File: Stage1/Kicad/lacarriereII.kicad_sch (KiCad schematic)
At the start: 75 parts, among them J1 USB_C_Receptacle_USB2.0, J2 Conn_02x06, J4 Conn_01x06_Pin, U1 PCA9557PW, U10 XC6206P132MR, U11 ESP32_WROVER, U13 BME280, U15 BME280, U2 BQ25171QWDRCRQ1, U3 CH340C, U4 UMH3N, U5 SIM800L-CORE, U6 FS8205, U7 HY2112, U8 TLV61070A, U9 XC6206P282MR

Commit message: [add] mounting holes + custom footprints lib
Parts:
- added H1, H2, H3: MountingHole_Pad, MountingHole:MountingHole_3.2mm_M3_Pad_Via, symbol Mechanical:MountingHole_Pad
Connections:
- net GND: now also H1.1, H2.1, H3.1
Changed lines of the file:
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@@
   (junction (at 167.64 170.18) (diameter 0) (color 0 0 0 0)
   )
+  (junction (at 259.08 246.38) (diameter 0) (color 0 0 0 0)
+  )
   (junction (at 76.2 187.96) (diameter 0) (color 0 0 0 0)
   )
@@
   (junction (at 392.43 167.64) (diameter 0) (color 0 0 0 0)
   )
+  (junction (at 266.7 246.38) (diameter 0) (color 0 0 0 0)
+  )
   (junction (at 22.86 227.33) (diameter 0) (color 0 0 0 0)
   )
@@
     (stroke (width 0) (type default))
   )
+  (wire (pts (xy 266.7 246.38) (xy 266.7 262.89))
+    (stroke (width 0) (type default))
+  )
   (wire (pts (xy 193.04 243.84) (xy 201.93 243.84))
     (stroke (width 0) (type default))
@@
     (stroke (width 0) (type default))
   )
+  (wire (pts (xy 266.7 246.38) (xy 266.7 242.57))
+    (stroke (width 0) (type default))
+  )
   (wire (pts (xy 54.61 242.57) (xy 73.66 242.57))
     (stroke (width 0) (type default))
@@
     (stroke (width 0) (type default))
   )
+  (wire (pts (xy 259.08 246.38) (xy 266.7 246.38))
+    (stroke (width 0) (type default))
+  )
   (wire (pts (xy 52.07 81.28) (xy 59.69 81.28))
     (stroke (width 0) (type default))
@@
     (stroke (width 0) (type default))
   )
+  (wire (pts (xy 259.08 246.38) (xy 259.08 242.57))
+    (stroke (width 0) (type default))
+  )
   (wire (pts (xy 167.64 167.64) (xy 167.64 170.18))
     (stroke (width 0) (type default))
@@
     (stroke (width 0) (type default))
   )
+  (wire (pts (xy 252.73 246.38) (xy 252.73 242.57))
+    (stroke (width 0) (type default))
+  )
   (wire (pts (xy 298.45 187.96) (xy 313.69 187.96))
     (stroke (width 0) (type default))
@@
     (stroke (width 0) (type default))
   )
+  (wire (pts (xy 252.73 246.38) (xy 259.08 246.38))
+    (stroke (width 0) (type default))
+  )
   (wire (pts (xy 118.11 74.93) (xy 118.11 73.66))
     (stroke (width 0) (type default))
@@
     )
   )
+  (symbol (lib_id "power:GND") (at 266.7 262.89 0) (unit 1)
+    (in_bom yes) (on_board yes) (dnp no) (fields_autoplaced)
+    (property "Reference" "#PWR016" (at 266.7 269.24 0)
+      (effects (font (size 1.27 1.27)) hide)
+    )
+    (property "Value" "GND" (at 266.7 267.97 0)
+      (effects (font (size 1.27 1.27)))
+    )
+    (property "Footprint" "" (at 266.7 262.89 0)
+      (effects (font (size 1.27 1.27)) hide)
+    )
+    (property "Datasheet" "" (at 266.7 262.89 0)
+      (effects (font (size 1.27 1.27)) hide)
+    )
+    (pin "1")
+    (instances
+      (project "lacarriereII"
+        (path "/3c8426f4-ef7d-418b-9048-6c57d75d81b5"
+          (reference "#PWR016") (unit 1)
+        )
+      )
+    )
+  )
   (symbol (lib_id "Device:Thermistor_NTC") (at 182.88 163.83 0) (unit 1)
     (in_bom yes) (on_board yes) (dnp no)
@@
     )
   )
+  (symbol (lib_id "Mechanical:MountingHole_Pad") (at 252.73 240.03 0) (unit 1)
+    (in_bom yes) (on_board yes) (dnp no)
+    (property "Reference" "H1" (at 255.27 238.125 0)
+      (effects (font (size 1.27 1.27)) (justify left))
+    )
+    (property "Value" "MountingHole_Pad" (at 261.62 238.76 0)
+      (effects (font (size 1.27 1.27)) (justify left) hide)
+    )
+    (property "Footprint" "MountingHole:MountingHole_3.2mm_M3_Pad_Via" (at 252.73 240.03 0)
+      (effects (font (size 1.27 1.27)) hide)
+    )
+    (property "Datasheet" "~" (at 252.73 240.03 0)
+      (effects (font (size 1.27 1.27)) hide)
+    )
+    (pin "1")
+    (instances
+      (project "lacarriereII"
+        (path "/3c8426f4-ef7d-418b-9048-6c57d75d81b5"
+          (reference "H1") (unit 1)
+        )
+      )
+    )
+  )
   (symbol (lib_id "Connector:TestPoint") (at 279.4 149.86 0) (unit 1)
     (in_bom yes) (on_board yes) (dnp no)
@@
     )
   )
+  (symbol (lib_id "Mechanical:MountingHole_Pad") (at 259.08 240.03 0) (unit 1)
+    (in_bom yes) (on_board yes) (dnp no) (fields_autoplaced)
+    (property "Reference" "H2" (at 261.62 238.125 0)
+      (effects (font (size 1.27 1.27)) (justify left))
+    )
+    (property "Value" "MountingHole_Pad" (at 261.62 240.665 0)
+      (effects (font (size 1.27 1.27)) (justify left) hide)
+    )
+    (property "Footprint" "MountingHole:MountingHole_3.2mm_M3_Pad_Via" (at 259.08 240.03 0)
+      (effects (font (size 1.27 1.27)) hide)
+    )
+    (property "Datasheet" "~" (at 259.08 240.03 0)
+      (effects (font (size 1.27 1.27)) hide)
+    )
+    (pin "1")
+    (instances
+      (project "lacarriereII"
+        (path "/3c8426f4-ef7d-418b-9048-6c57d75d81b5"
+          (reference "H2") (unit 1)
+        )
+      )
+    )
+  )
   (symbol (lib_id "Device:L") (at 220.98 142.24 90) (unit 1)
     (in_bom yes) (on_board yes) (dnp no)
@@
         )
       )
+    )
+  )
+  (symbol (lib_id "Mechanical:MountingHole_Pad") (at 266.7 240.03 0) (unit 1)
+    (in_bom yes) (on_board yes) (dnp no) (fields_autoplaced)
+    (property "Reference" "H3" (at 269.24 238.125 0)
+      (effects (font (size 1.27 1.27)) (justify left))
+    )
+    (property "Value" "MountingHole_Pad" (at 269.24 240.665 0)
+      (effects (font (size 1.27 1.27)) (justify left) hide)
+    )
+    (property "Footprint" "MountingHole:MountingHole_3.2mm_M3_Pad_Via" (at 266.7 240.03 0)
+      (effects (font (size 1.27 1.27)) hide)
+    )
+    (property "Datasheet" "~" (at 266.7 240.03 0)
+      (effects (font (size 1.27 1.27)) hide)
+    )
+    (pin "1")
+    (instances
+      (project "lacarriereII"
+        (path "/3c8426f4-ef7d-418b-9048-6c57d75d81b5"
+          (reference "H3") (unit 1)
+        )
+      )

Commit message: [update] Stage1 schematic after olli's review
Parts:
- removed C20: 1u(nc), Capacitor_SMD:C_0805_2012Metric_Pad1.18x1.45mm_HandSolder, symbol Device:C
- removed R26: 1M, Resistor_SMD:R_0805_2012Metric_Pad1.20x1.40mm_HandSolder, symbol Meteo_Lacarriere:R
- removed U13, U15: BME280, Package_LGA:Bosch_LGA-8_2.5x2.5mm_P0.65mm_ClockwisePinNumbering, symbol Meteo_Lacarriere:BME280
- added C11: NC(1u), Capacitor_SMD:C_0805_2012Metric_Pad1.18x1.45mm_HandSolder, symbol Device:C
- added C13, C14: 1u, Capacitor_SMD:C_0805_2012Metric_Pad1.18x1.45mm_HandSolder, symbol Device:C
- added C21, C23, C24, C3: 0.1u, Capacitor_SMD:C_0805_2012Metric_Pad1.18x1.45mm_HandSolder, symbol Device:C
- added R1: 10k, Resistor_SMD:R_0805_2012Metric_Pad1.20x1.40mm_HandSolder, symbol Meteo_Lacarriere:R
- added R2: 10k, Resistor_SMD:R_0805_2012Metric_Pad1.20x1.40mm_HandSolder, symbol Device:R
- added R24: 1M, Resistor_SMD:R_0805_2012Metric_Pad1.20x1.40mm_HandSolder, symbol Meteo_Lacarriere:R
- added U14, U16: BME280, Package_LGA:Bosch_LGA-8_2.5x2.5mm_P0.65mm_ClockwisePinNumbering, symbol Meteo_Lacarriere:BME280
- added U2: USBLC6-2SC6, Package_TO_SOT_SMD:SOT-23-6_Handsoldering, symbol Meteo_Lacarriere:USBLC6-2SC6
- TH1: value NTC -> NC(NTC)
- renumbered 1V3 to 1V1, 2V8 to 2V1, 3V3 to 3V1, C3 to C1, C11 to C12, C12 to C15, C13 to C16, C14 to C17, C15 to C18, C1 to C19, C16 to C20, C17 to C22, C18 to C25, C19 to C26, J4 to J3, R7 to R10, R8 to R11, R11 to R12, R14 to R13, R12 to R14, R13 to R15, R17 to R16, R15 to R17, R16 to R18, R18 to R19, R19 to R20, R20 to R21, R27 to R22, R25 to R23, R21 to R25, R22 to R26, R23 to R27, R24 to R28, R2 to R5, R9 to R6, R10 to R7, R5 to R8, R6 to R9, U9 to U10, U10 to U11, U11 to U12, U12 to U13, U14 to U15, U16 to U17, U2 to U3, U3 to U4, U4 to U6, U6 to U7, U7 to U8, U8 to U9
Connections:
- net IO0 is gone; now on net IO0_AND_D5: U12.25 (IO0), U6.3 (C2)
- net +3.3V: now also R25.1, R26.2, C13.1, C14.1, C21.1, C23.1, C24.1, C3.1, R1.1, R2.2, U14.2 (~{CS}), U14.6 (VDDIO), U14.8 (VDD), U16.2 (~{CS}), U16.5 (SDO), U16.6 (VDDIO), U16.8 (VDD), U2.5 (VBUS)
- net D3: now also U12.24 (IO2); no longer U12.23 (IO15)
- net DVP_SCL: now also R26.1; no longer R26.2
- net DVP_SDA: now also R25.2; no longer R25.1
- net GND: now also J1.S1 (SHIELD), C11.2, C13.2, C14.2, C21.2, C23.2, C24.2, C3.2, R24.2, U14.1 (GND1), U14.5 (SDO), U14.7 (GND2), U16.1 (GND1), U16.7 (GND2), U2.2 (GND); no longer R25.2, R26.1
- net I2C_SCL: now also R1.2, U14.4 (SCL), U16.4 (SCL)
- net I2C_SDA: now also R2.1, U14.3 (SDA), U16.3 (SDA)
- net VMEAS: now also C11.1, R24.1
- net at R6.2: now also U2.1 (I/O1_1); no longer U4.5 (UD+)
- net IO_EXT2: now reaches J2.11 (Pin_11)
- net IO_EXT2: now also J2.5 (Pin_5), U12.23 (IO15)
- net at U4.6 (UD-): now also U2.4 (I/O2_2); no longer R7.2
- net D5 renamed IO0_AND_D5
- net IO0_AND_D5: no longer U12.37 (IO23)
- net IO2 renamed IO_EXT1
- net IO_EXT1: now also U12.37 (IO23); no longer U12.24 (IO2)
- new net: U2.6 (I/O1_2), U4.5 (UD+)
- new net: R7.2, U2.3 (I/O2_1)
- no-connect marks 13 -> 10
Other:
- note added: "Dual Bosh sensors"
- note added: "Manual jumper selection"
- note added: "R22 populated if no NTC"
- note added: "R27=((Vout/Vref)-1)*R28 R27=((4.1/0.5)-1)*R28 R27=100k ; R28=14k"
- note added: "R3 = 750R ; Charging 0.4A R9=0 ; R10=NC ; NO TEMPERATURE MANAGEMENT R13=62k ; Li+ No Timer R16=100k ; LiFePo4 3.5V charging"
- note added: "USB C 2.0 & Serial programmer"
- note added: "Voltage divider (VMEAS, PIN 4) on ADC1 as ADC2 is OFF when Wifi is active"
- note removed: "Double Bosh sensors"
- note removed: "Manual input selection"
- note removed: "Pont diviseur (VMEAS, PIN 4) sur ADC1 car ADC2 OFF quand WIFI actif"
- note removed: "R23=((Vout/Vref)-1)*R24 R23=((4.1/0.5)-1)*R24 R23=82k ; R24=11.5k L1 74438357022 from Wurth trouver equivalent ?"
- note removed: "R27 populated if no NTC"
- note removed: "R6 = 375R ; Charging 0.8A R10=0 ; R11=NC ; TEMP 0°C to 40°C R16=62k ; Li+ No Timer R17=100k ; LiFePo4 3.5V charging"
- note removed: "USB C & Serial programmer"
- moved on the sheet: 1V1, 2V1, 3V1, 4V1, C1, C15, C16, C17, C18, C19, C2, C20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

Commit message: [fix] a few mistakes on schematic ... ready to reroute!
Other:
- note added: "I2C general pull-ups"
- moved on the sheet: H1, H2, H3, R1, R2, R8, R9, U1

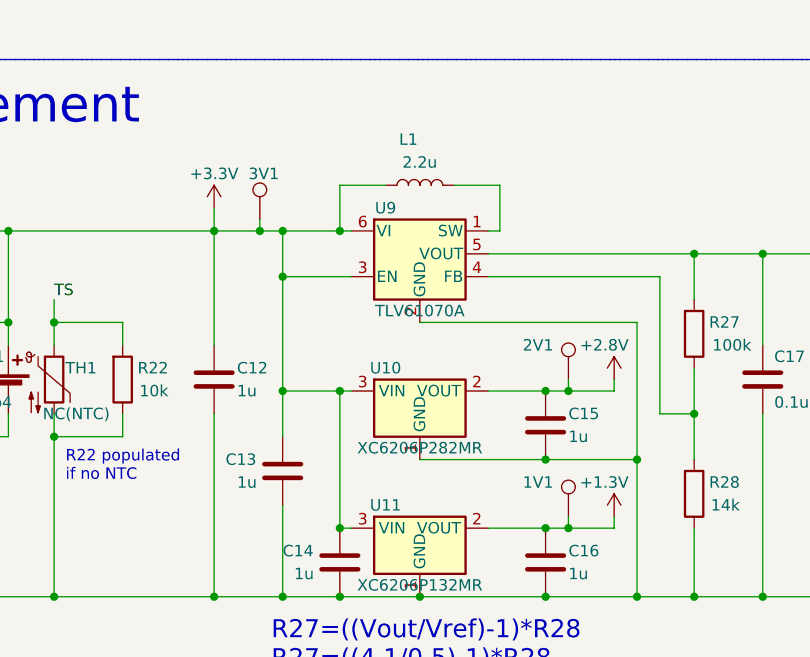
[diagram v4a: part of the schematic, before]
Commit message: [reroute] pcb board after oli's review
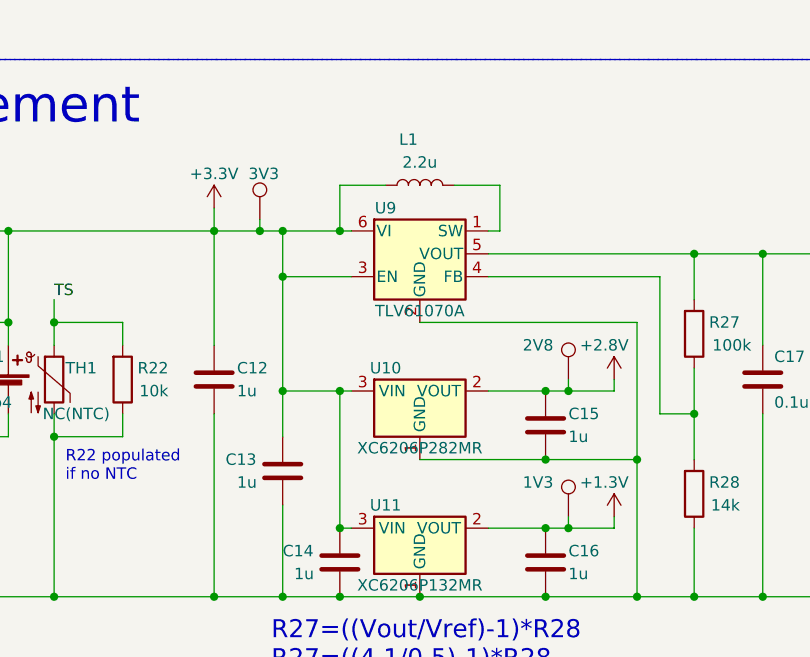
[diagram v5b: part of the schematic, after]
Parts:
- renumbered 1V1 to 1V3, 2V1 to 2V8, 3V1 to 3V3
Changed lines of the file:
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@@
   (symbol (lib_id "Connector:TestPoint") (at 240.03 163.83 0) (unit 1)
     (in_bom yes) (on_board yes) (dnp no)
-    (property "Reference" "2V1" (at 234.95 160.02 0)
+    (property "Reference" "2V8" (at 234.95 160.02 0)
       (effects (font (size 1.27 1.27)) (justify left))
     )
@@
       (project "lacarriereII"
         (path "/3c8426f4-ef7d-418b-9048-6c57d75d81b5"
-          (reference "2V1") (unit 1)
+          (reference "2V8") (unit 1)
         )
       )
@@
   (symbol (lib_id "Connector:TestPoint") (at 205.74 146.05 0) (unit 1)
     (in_bom yes) (on_board yes) (dnp no)
-    (property "Reference" "3V1" (at 204.47 140.97 0)
+    (property "Reference" "3V3" (at 204.47 140.97 0)
       (effects (font (size 1.27 1.27)) (justify left))
     )
@@
       (project "lacarriereII"
         (path "/3c8426f4-ef7d-418b-9048-6c57d75d81b5"
-          (reference "3V1") (unit 1)
+          (reference "3V3") (unit 1)
         )
       )
@@
   (symbol (lib_id "Connector:TestPoint") (at 240.03 179.07 0) (unit 1)
     (in_bom yes) (on_board yes) (dnp no)
-    (property "Reference" "1V1" (at 234.95 175.26 0)
+    (property "Reference" "1V3" (at 234.95 175.26 0)
       (effects (font (size 1.27 1.27)) (justify left))
     )
@@
       (project "lacarriereII"
         (path "/3c8426f4-ef7d-418b-9048-6c57d75d81b5"
-          (reference "1V1") (unit 1)
-        )
-      )
+          (reference "1V3") (unit 1)
+        )
+      )
